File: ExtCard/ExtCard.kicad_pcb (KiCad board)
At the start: 2 copper layers, 62.2 x 57.2 mm, 36 parts, among them J1 WIZNET, J3 EXTSPI, Q1 2N3906, Q2 2N3906, Q3 2N3906, U12 MicroSD_SPI_CD, U13 MicroSD_SPI_CD

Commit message: Moved around some traces
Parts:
- R1, R4: value 1k -> 10k
- R2, R3, R5: value 10k -> 100k
- moved C7 12.7 mm to (108.0, 104.3), turned to 90 degrees
- moved D5 8.19 mm to (111.0, 88.3), turned to -90 degrees
- moved R33 7.92 mm to (100.9, 96.2), turned to 90 degrees
- moved D9 7.61 mm to (97.6, 95.9)
- moved R30 7.10 mm to (90.0, 89.0)
- moved D7 5.35 mm to (111.2, 135.7), turned to -90 degrees
- moved Q1 5.15 mm to (101.4, 129.0), turned to 90 degrees
- moved D3 2.87 mm to (73.4, 126.9), turned to 180 degrees
- moved D8 0.61 mm to (97.6, 92.6)
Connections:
- D3 pad 1: GND -> Net-(Q2-Pad1)
- D3 pad 2: Net-(D3-Pad2) -> +5V
- D5 pad 1: GND -> Net-(D5-Pad1)
- D5 pad 2: Net-(D5-Pad2) -> +5V
- D7 pad 1: GND -> Net-(Q1-Pad1)
- D7 pad 2: Net-(R32-Pad2) -> +5V
- Q1 pad 1: +5V -> Net-(Q1-Pad1)
- Q2 pad 1: +5V -> Net-(Q2-Pad1)
- Q3 pad 1: +5V -> Net-(D5-Pad1)
- R23 pad 2: Net-(D3-Pad2) -> GND
- R30 pad 2: Net-(D5-Pad2) -> GND
- R32 pad 2: Net-(R32-Pad2) -> GND
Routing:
- net Net-(D5-Pad1): track 0.00 -> 28.1 mm
- net Net-(Q2-Pad1): track 0.00 -> 15.9 mm
- net Net-(C6-Pad2): track 46.8 -> 62.6 mm
- net Net-(Q1-Pad1): track 0.00 -> 12.5 mm
- net Net-(D5-Pad2): track 9.58 -> 0.00 mm
- net +5V: track 128.9 -> 136.8 mm
- net Net-(D3-Pad2): track 6.13 -> 0.00 mm
- net Net-(R32-Pad2): track 5.08 -> 0.00 mm
- net Net-(Q3-Pad3): track 10.5 -> 6.99 mm
- net Net-(C7-Pad2): track 34.1 -> 30.9 mm
- net Net-(Q1-Pad3): track 11.4 -> 8.36 mm
- net Net-(Q1-Pad2): track 5.77 -> 5.26 mm

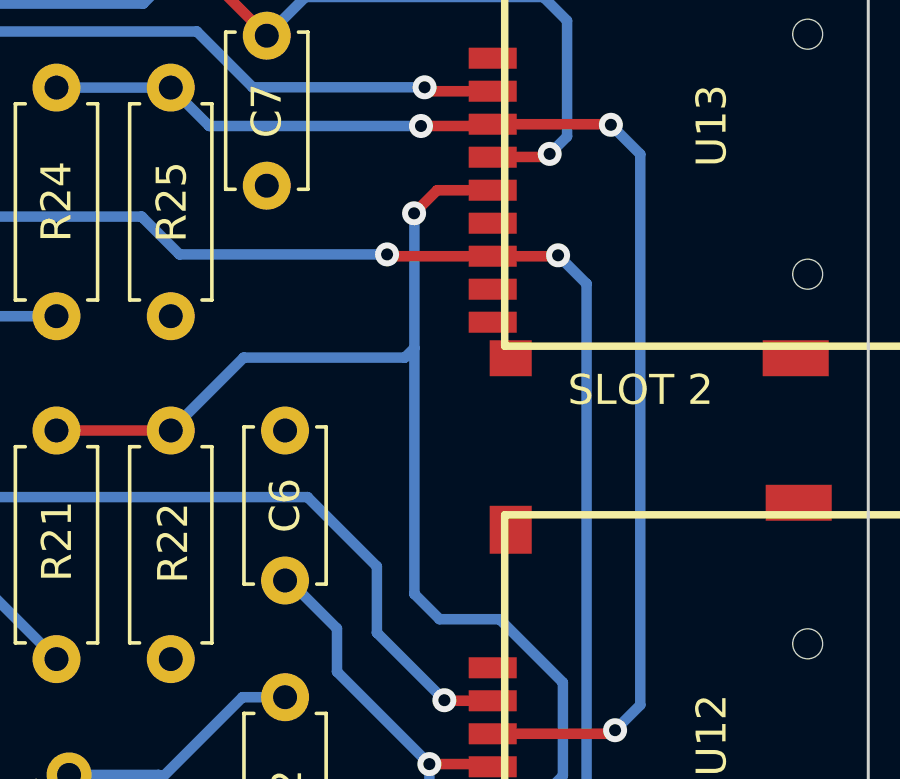
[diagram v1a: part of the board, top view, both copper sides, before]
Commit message: Added 16k/32k jumper
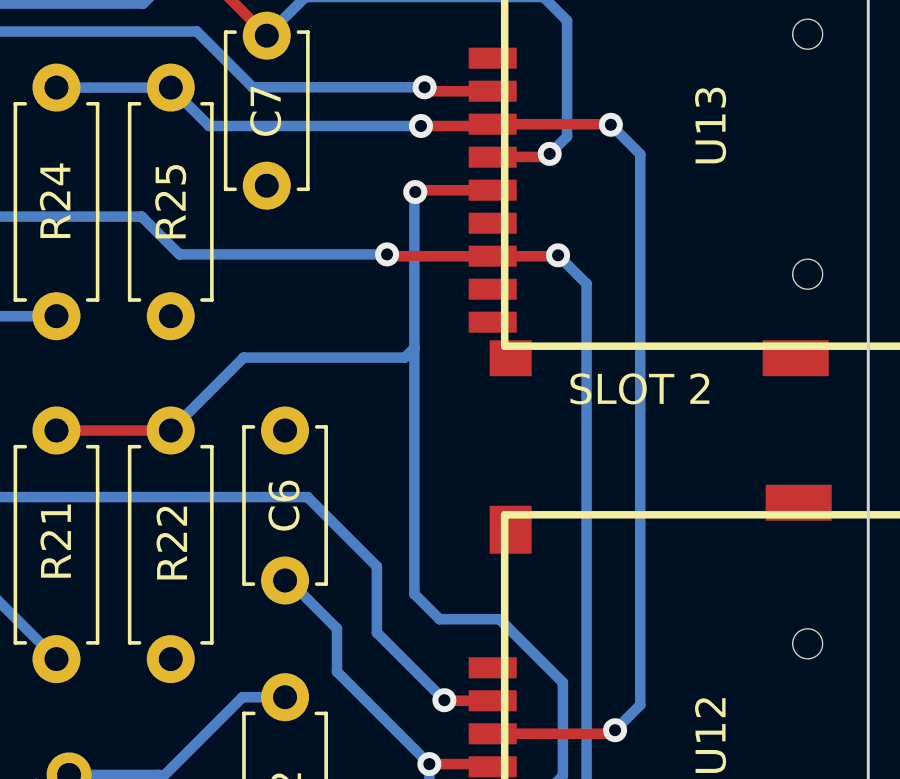
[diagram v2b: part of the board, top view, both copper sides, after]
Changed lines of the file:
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@@
   (segment (start 101.42 126.47) (end 99.68 126.47) (width 0.35) (layer "B.Cu") (net 23))
   (segment (start 104.81 112.45) (end 101 112.45) (width 0.35) (layer "F.Cu") (net 24))
-  (segment (start 113.69 104.44) (end 115.54 104.44) (width 0.35) (layer "F.Cu") (net 24))
+  (segment (start 112.96 104.5) (end 113.02 104.44) (width 0.35) (layer "F.Cu") (net 24))
   (segment (start 115.56 124.78) (end 115.54 124.76) (width 0.35) (layer "F.Cu") (net 24))
   (segment (start 117.37 124.47) (end 117.06 124.78) (width 0.35) (layer "F.Cu") (net 24))
-  (segment (start 112.92 105.21) (end 113.69 104.44) (width 0.35) (layer "F.Cu") (net 24))
   (segment (start 117.06 124.78) (end 115.56 124.78) (width 0.35) (layer "F.Cu") (net 24))
+  (segment (start 113.02 104.44) (end 115.54 104.44) (width 0.35) (layer "F.Cu") (net 24))
   (via (at 117.37 124.47) (size 0.8) (drill 0.4) (layers "F.Cu" "B.Cu") (net 24))
-  (via (at 112.92 105.21) (size 0.8) (drill 0.4) (layers "F.Cu" "B.Cu") (net 24))
-  (segment (start 112.92 105.21) (end 112.93 105.22) (width 0.35) (layer "B.Cu") (net 24))
+  (via (at 112.96 104.5) (size 0.8) (drill 0.4) (layers "F.Cu" "B.Cu") (net 24))
+  (segment (start 107.24 110.02) (end 112.61 110.02) (width 0.35) (layer "B.Cu") (net 24))
+  (segment (start 104.81 112.45) (end 107.24 110.02) (width 0.35) (layer "B.Cu") (net 24))
+  (segment (start 112.93 104.53) (end 112.93 117.9) (width 0.35) (layer "B.Cu") (net 24))
   (segment (start 112.93 117.9) (end 113.77 118.74) (width 0.35) (layer "B.Cu") (net 24))
-  (segment (start 107.24 110.02) (end 112.61 110.02) (width 0.35) (layer "B.Cu") (net 24))
+  (segment (start 112.61 110.02) (end 112.93 109.7) (width 0.35) (layer "B.Cu") (net 24))
   (segment (start 117.88 123.96) (end 117.37 124.47) (width 0.35) (layer "B.Cu") (net 24))
-  (segment (start 104.81 112.45) (end 107.24 110.02) (width 0.35) (layer "B.Cu") (net 24))
-  (segment (start 112.93 105.22) (end 112.93 117.9) (width 0.35) (layer "B.Cu") (net 24))
   (segment (start 115.77 118.74) (end 117.88 120.85) (width 0.35) (layer "B.Cu") (net 24))
-  (segment (start 112.61 110.02) (end 112.93 109.7) (width 0.35) (layer "B.Cu") (net 24))
   (segment (start 113.77 118.74) (end 115.77 118.74) (width 0.35) (layer "B.Cu") (net 24))
+  (segment (start 112.96 104.5) (end 112.93 104.53) (width 0.35) (layer "B.Cu") (net 24))
   (segment (start 117.88 120.85) (end 117.88 123.96) (width 0.35) (layer "B.Cu") (net 24))
   (segment (start 119.5 122.56) (end 119.62 122.44) (width 0.35) (layer "F.Cu") (net 25))
